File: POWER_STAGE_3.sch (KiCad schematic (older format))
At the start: 13 parts, among them IC661 BTN8962TA

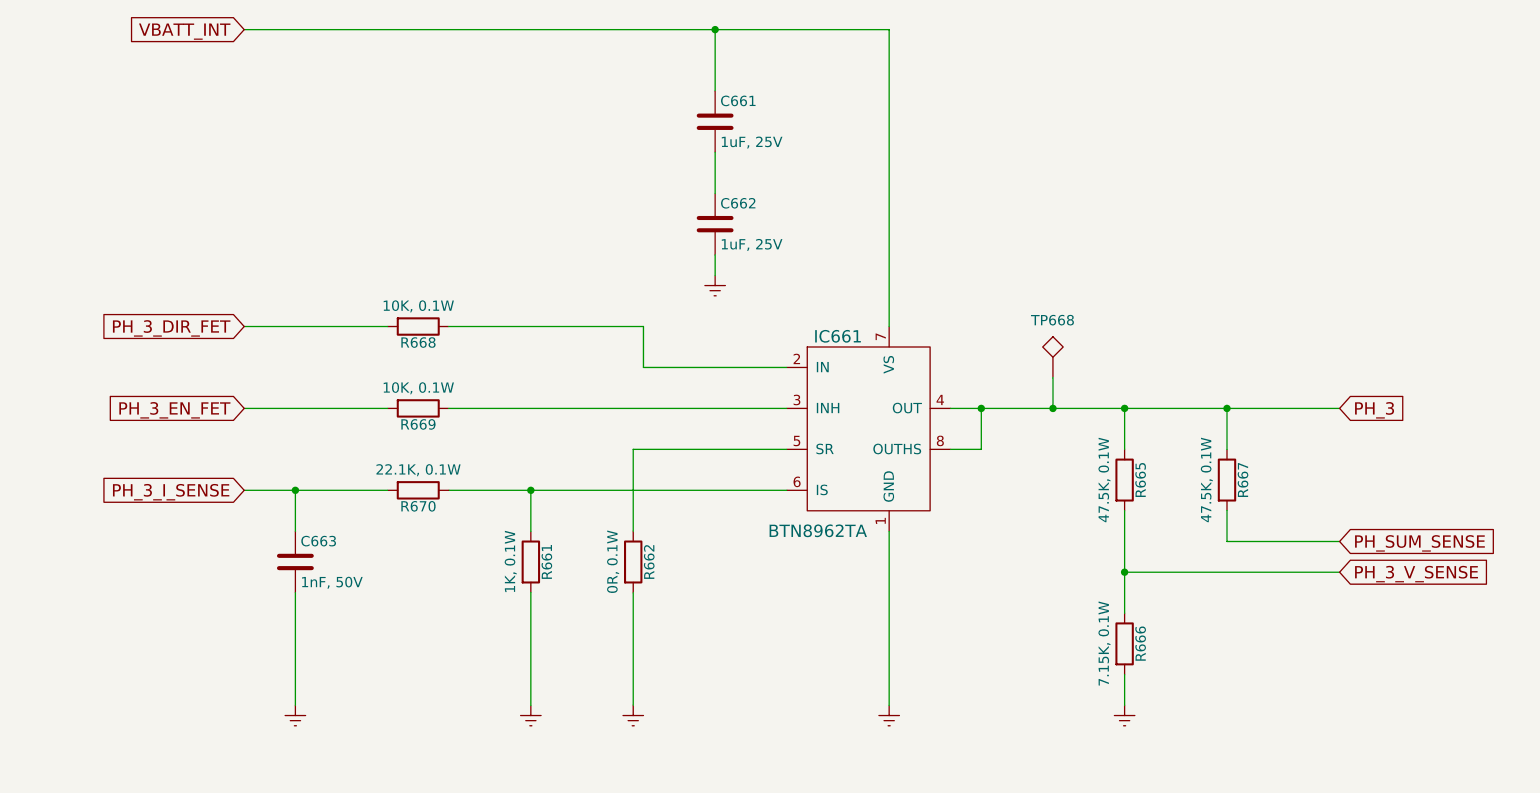
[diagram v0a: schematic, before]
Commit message: - Finished adaptation to JMS board footprint. - Added testpoints. - Changed header connector to 0.1" pitch, and tall.
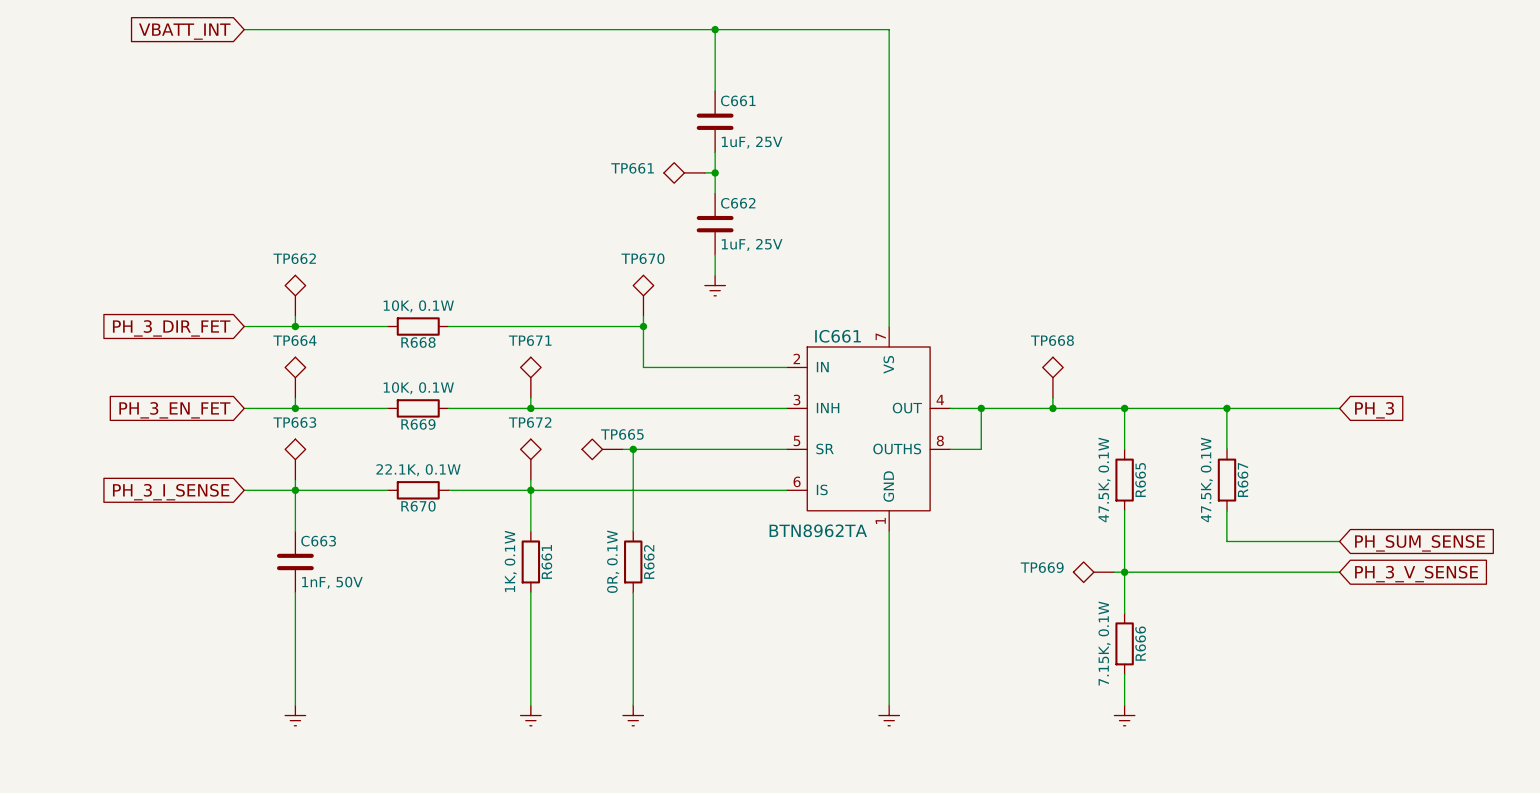
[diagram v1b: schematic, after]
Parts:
- added TP661, TP662, TP663, TP664, TP665, TP669, TP670, TP671, TP672: TEST, hp-bldc-pcb:TEST_POINT_40mil, symbol TEST
- TP668: footprint Measurement_Points:Measurement_Point_Round-SMD-Pad_Big -> hp-bldc-pcb:TEST_POINT_40mil
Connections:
- net PH_3_DIR_FET: now also TP662.1
- net PH_3_EN_FET: now also TP664.1
- net PH_3_I_SENSE: now also TP663.1
- net PH_3_V_SENSE: now also TP669.1
- net at IC661.2 (IN), R668.1: now also TP670.1
- net at IC661.3 (INH), R669.1: now also TP671.1
- net at IC661.5 (SR), R662.1: now also TP665.1
- net at IC661.6 (IS), R661.1, R670.1: now also TP672.1
- net at C661.2, C662.1: now also TP661.1
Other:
- moved on the sheet: TP668
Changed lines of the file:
@@
 	4050 3250 5000 3250
 Wire Wire Line
-	5000 3250 5000 3450
+	5000 3200 5000 3450
 Wire Wire Line
 	5000 3450 5700 3450
@@
 $EndComp
 Wire Wire Line
-	3300 4250 3300 4050
+	3300 4000 3300 4250
 Connection ~ 3300 4050
 $Comp
-L Earth #PWR049
+L Earth #PWR050
 U 1 1 5A7A4873
 P 3300 5100
-F 0 "#PWR049" H 3300 4850 50  0001 C CNN
+F 0 "#PWR050" H 3300 4850 50  0001 C CNN
 F 1 "Earth" H 3300 4950 50  0001 C CNN
 F 2 "" H 3300 5100 50  0001 C CNN
@@
 $EndComp
 Wire Wire Line
-	4450 4250 4450 4050
+	4450 4000 4450 4250
 Connection ~ 4450 4050
 Wire Wire Line
 	4950 4250 4950 3850
 Wire Wire Line
-	4950 3850 5700 3850
-$Comp
-L Earth #PWR050
+	4900 3850 5700 3850
+$Comp
+L Earth #PWR051
 U 1 1 5A7A488C
 P 4450 5100
-F 0 "#PWR050" H 4450 4850 50  0001 C CNN
+F 0 "#PWR051" H 4450 4850 50  0001 C CNN
 F 1 "Earth" H 4450 4950 50  0001 C CNN
 F 2 "" H 4450 5100 50  0001 C CNN
@@
 	4450 4550 4450 5100
 $Comp
-L Earth #PWR051
+L Earth #PWR052
 U 1 1 5A7A4893
 P 4950 5100
-F 0 "#PWR051" H 4950 4850 50  0001 C CNN
+F 0 "#PWR052" H 4950 4850 50  0001 C CNN
 F 1 "Earth" H 4950 4950 50  0001 C CNN
 F 2 "" H 4950 5100 50  0001 C CNN
@@
 	4950 4550 4950 5100
 $Comp
-L Earth #PWR052
+L Earth #PWR053
 U 1 1 5A7A489A
 P 6200 5100
-F 0 "#PWR052" H 6200 4850 50  0001 C CNN
+F 0 "#PWR053" H 6200 4850 50  0001 C CNN
 F 1 "Earth" H 6200 4950 50  0001 C CNN
 F 2 "" H 6200 5100 50  0001 C CNN
@@
 $EndComp
 $Comp
-L Earth #PWR053
+L Earth #PWR054
 U 1 1 5A7A48AF
 P 5350 3000
-F 0 "#PWR053" H 5350 2750 50  0001 C CNN
+F 0 "#PWR054" H 5350 2750 50  0001 C CNN
 F 1 "Earth" H 5350 2850 50  0001 C CNN
 F 2 "" H 5350 3000 50  0001 C CNN
@@
 PH_3_V_SENSE
 Wire Wire Line
-	8400 4450 7350 4450
+	7300 4450 8400 4450
 Connection ~ 7350 4450
 $Comp
-L Earth #PWR054
+L Earth #PWR055
 U 1 1 5A7A48E1
 P 7350 5100
-F 0 "#PWR054" H 7350 4850 50  0001 C CNN
+F 0 "#PWR055" H 7350 4850 50  0001 C CNN
 F 1 "Earth" H 7350 4950 50  0001 C CNN
 F 2 "" H 7350 5100 50  0001 C CNN
@@
 L TEST TP668
 U 1 1 5A7A48E8
-P 7000 3500
-F 0 "TP668" H 7000 3750 50  0000 C BNN
-F 1 "TEST" H 7000 3750 50  0001 C CNN
-F 2 "Measurement_Points:Measurement_Point_Round-SMD-Pad_Big" H 7000 3500 50  0001 C CNN
-F 3 "" H 7000 3500 50  0001 C CNN
-	1    7000 3500
-	1    0    0    -1
-$EndComp
-Wire Wire Line
-	7000 3500 7000 3650
+P 7000 3600
+F 0 "TP668" H 7000 3850 50  0000 C BNN
+F 1 "TEST" H 7000 3850 50  0001 C CNN
+F 2 "hp-bldc-pcb:TEST_POINT_40mil" H 7000 3600 50  0001 C CNN
+F 3 "" H 7000 3600 50  0001 C CNN
+	1    7000 3600
+	1    0    0    -1
+$EndComp
+Wire Wire Line
+	7000 3600 7000 3650
 Connection ~ 7000 3650
+$Comp
+L TEST TP662
+U 1 1 5AB3CC4B
+P 3300 3200
+F 0 "TP662" H 3300 3450 50  0000 C BNN
+F 1 "TEST" H 3300 3450 50  0001 C CNN
+F 2 "hp-bldc-pcb:TEST_POINT_40mil" H 3300 3200 50  0001 C CNN
+F 3 "" H 3300 3200 50  0001 C CNN
+	1    3300 3200
+	1    0    0    -1
+$EndComp
+$Comp
+L TEST TP664
+U 1 1 5AB3CC70
+P 3300 3600
+F 0 "TP664" H 3300 3850 50  0000 C BNN
+F 1 "TEST" H 3300 3850 50  0001 C CNN
+F 2 "hp-bldc-pcb:TEST_POINT_40mil" H 3300 3600 50  0001 C CNN
+F 3 "" H 3300 3600 50  0001 C CNN
+	1    3300 3600
+	1    0    0    -1
+$EndComp
+$Comp
+L TEST TP663
+U 1 1 5AB3CCBD
+P 3300 4000
+F 0 "TP663" H 3300 4250 50  0000 C BNN
+F 1 "TEST" H 3300 4250 50  0001 C CNN
+F 2 "hp-bldc-pcb:TEST_POINT_40mil" H 3300 4000 50  0001 C CNN
+F 3 "" H 3300 4000 50  0001 C CNN
+	1    3300 4000
+	1    0    0    -1
+$EndComp
+Wire Wire Line
+	3300 3200 3300 3250
+Connection ~ 3300 3250
+Wire Wire Line
+	3300 3600 3300 3650
+Connection ~ 3300 3650
+$Comp
+L TEST TP670
+U 1 1 5AB3CE32
+P 5000 3200
+F 0 "TP670" H 5000 3450 50  0000 C BNN
+F 1 "TEST" H 5000 3450 50  0001 C CNN
+F 2 "hp-bldc-pcb:TEST_POINT_40mil" H 5000 3200 50  0001 C CNN
+F 3 "" H 5000 3200 50  0001 C CNN
+	1    5000 3200
+	1    0    0    -1
+$EndComp
+$Comp
+L TEST TP671
+U 1 1 5AB3CE8D
+P 4450 3600
+F 0 "TP671" H 4450 3850 50  0000 C BNN
+F 1 "TEST" H 4450 3850 50  0001 C CNN
+F 2 "hp-bldc-pcb:TEST_POINT_40mil" H 4450 3600 50  0001 C CNN
+F 3 "" H 4450 3600 50  0001 C CNN
+	1    4450 3600
+	1    0    0    -1
+$EndComp
+$Comp
+L TEST TP672
+U 1 1 5AB3CEE3
+P 4450 4000
+F 0 "TP672" H 4450 4250 50  0000 C BNN
+F 1 "TEST" H 4450 4250 50  0001 C CNN
+F 2 "hp-bldc-pcb:TEST_POINT_40mil" H 4450 4000 50  0001 C CNN
+F 3 "" H 4450 4000 50  0001 C CNN
+	1    4450 4000
+	1    0    0    -1
+$EndComp
+Connection ~ 5000 3250
+Wire Wire Line
+	4450 3600 4450 3650
+Connection ~ 4450 3650
+$Comp
+L TEST TP661
+U 1 1 5AB3D082
+P 5300 2500
+F 0 "TP661" V 5350 2850 50  0000 C BNN
+F 1 "TEST" H 5300 2750 50  0001 C CNN
+F 2 "hp-bldc-pcb:TEST_POINT_40mil" H 5300 2500 50  0001 C CNN
+F 3 "" H 5300 2500 50  0001 C CNN
+	1    5300 2500
+	0    -1   -1   0
+$EndComp
+Wire Wire Line
+	5300 2500 5350 2500
+Connection ~ 5350 2500
+$Comp
+L TEST TP665
+U 1 1 5AB3D229
+P 4900 3850
+F 0 "TP665" V 5000 3850 50  0000 C BNN
+F 1 "TEST" H 4900 4100 50  0001 C CNN
+F 2 "hp-bldc-pcb:TEST_POINT_40mil" H 4900 3850 50  0001 C CNN
+F 3 "" H 4900 3850 50  0001 C CNN
+	1    4900 3850
+	0    -1   -1   0
+$EndComp
+Connection ~ 4950 3850
+$Comp
+L TEST TP669
+U 1 1 5AB3D80C
+P 7300 4450
+F 0 "TP669" V 7350 4800 50  0000 C BNN
+F 1 "TEST" H 7300 4700 50  0001 C CNN
+F 2 "hp-bldc-pcb:TEST_POINT_40mil" H 7300 4450 50  0001 C CNN
+F 3 "" H 7300 4450 50  0001 C CNN
+	1    7300 4450
+	0    -1   -1   0
+$EndComp
 $EndSCHEMATC

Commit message: - Minor changes to silkscreen. - Minor changes to BOM. - Additions to Readme file. - Page layout changed in schematic.
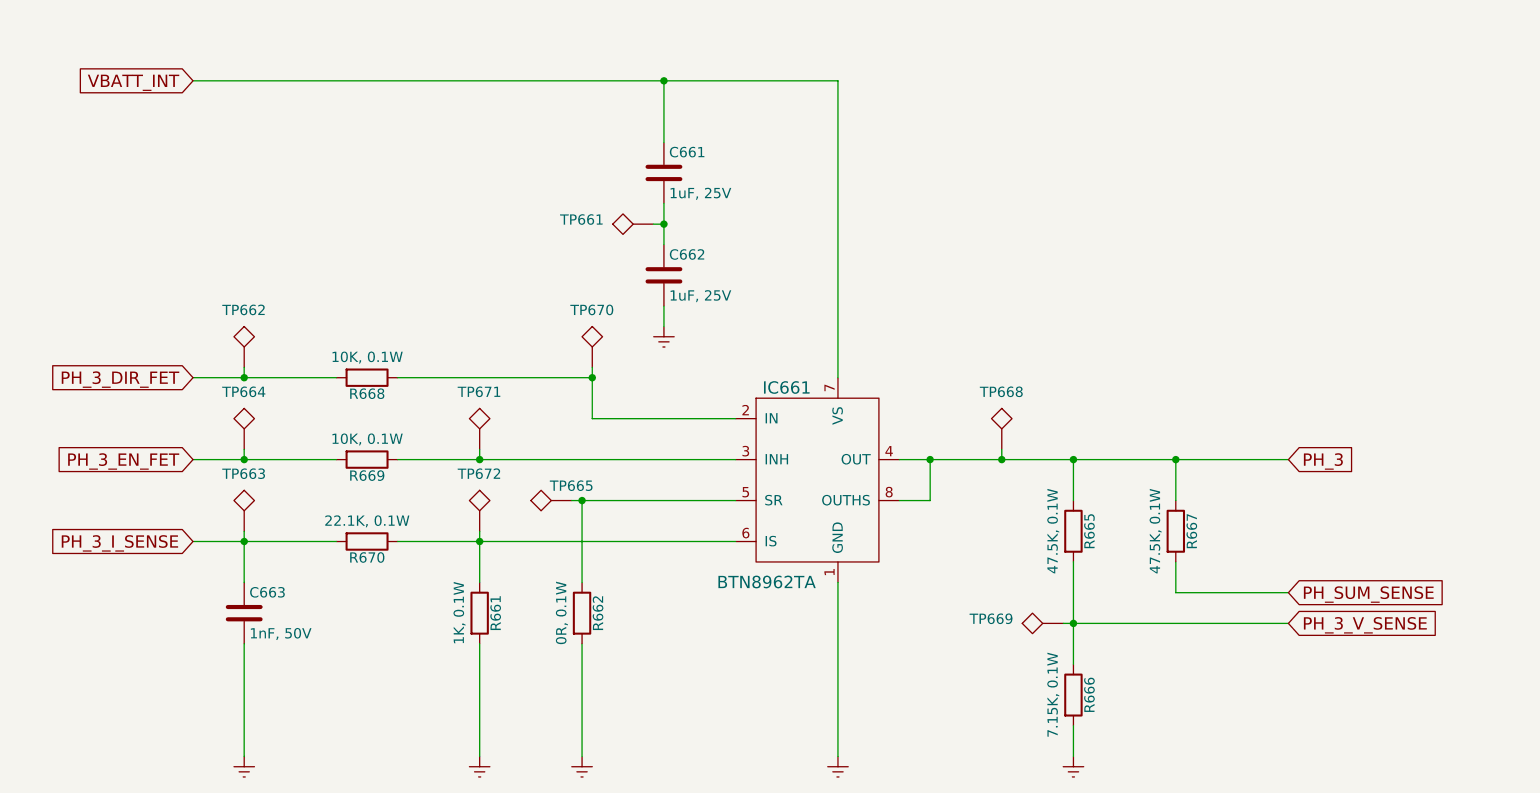
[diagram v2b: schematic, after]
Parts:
- IC661: footprint TO_SOT_Packages_SMD:TO-263-7_TabPin8 -> hp-bldc-pcb:TO-263-7_TabPin8
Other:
- moved on the sheet: C661, C662, C663, IC661, R661, R662, R665, R666, R667, R668, R669, R670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
